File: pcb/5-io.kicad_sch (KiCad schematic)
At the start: 0 parts

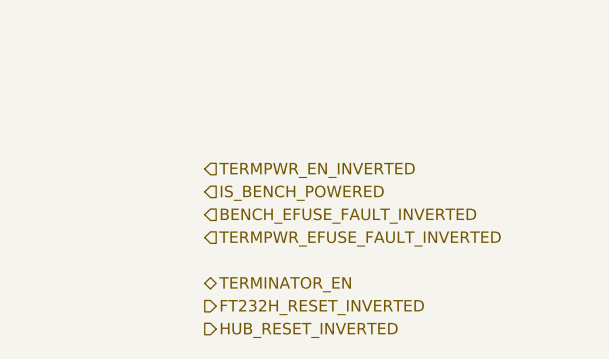
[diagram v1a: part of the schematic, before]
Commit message: Phase 3: populate SCSI sheet and channel sheets
SCSI sheet (A2): IDC50 and HD50 wired by signal name from SCSI-2
Table 2, all four RESERVED lines grounded through 0R links, the
logic-analyzer header as a pin-for-pin copy of the Digital Discovery
DIN connector, three SN74LVTH245A terminators with their DIP-switch
enable and truth table, and one cluster per line: 2 x 220R terminator
pair, ESD diode and channel sheet. Channel sheets hold the FDV301N
driver and the 74LVC1G17 receiver; 18 instances, references page x 100.

Generator: repeated sheets, sheet symbols, native tables, and
deterministic UUIDs. Nets renamed: LA -> LOGIC_ANALYZER,
TERMINATOR_EN -> TERMINATOR_EN_INVERTED_FIRMWARE.
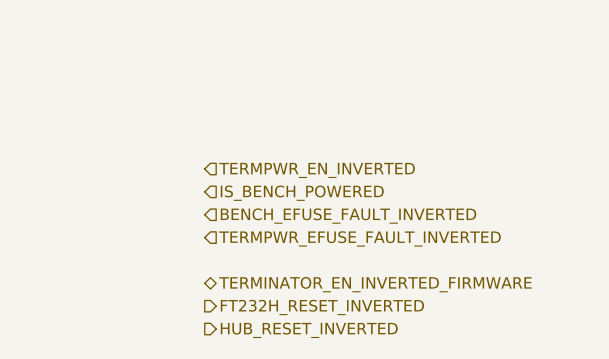
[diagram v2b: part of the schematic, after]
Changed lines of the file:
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@@
 		)
 	)
-	(hierarchical_label "TERMINATOR_EN"
+	(hierarchical_label "TERMINATOR_EN_INVERTED_FIRMWARE"
 		(shape bidirectional)
 		(at 343.8 63.5 0)
